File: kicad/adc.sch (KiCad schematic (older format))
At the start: 88 parts, among them IC501 TPD4E001, IC502 TPD4E001, IC503 TPD4E001, IC504 TPD4E001, IC505 TPD4E001, IC506 TPD4E001, U13_501 OPA4350EA/250, U13_502 OPA4350EA/250, U13_503 OPA4350EA/250, U13_504 OPA4350EA/250, U502 REF5030IDGKT, U503 OPA4350EA/250, U6_501 REF5030IDGKT

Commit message: usb interface changed by emu_interface
I've cleaned all the jtag interface, so the only things that go out is
jtag HOT and rx/tx isolated. I left the isolator for rx/tx cose I'm
planning to add rs485 using the same isolator and regulator, if not, I'd
clean these IC's also
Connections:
- net labels added: VDD3V3
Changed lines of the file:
@@
 EESchema Schematic File Version 4
-LIBS:servo-cache
 EELAYER 26 0
 EELAYER END
 $Descr B 17000 11000
 encoding utf-8
-Sheet 5 7
+Sheet 4 6
 Title "adc"
 Date "25 10 2019"
@@
 	10050 6200 10050 5200
 $Comp
-L servo:VDD #PWR0510
+L servo:VDD3V3 #PWR0510
 U 1 1 5DB391CF
 P 11400 2350
 F 0 "#PWR0510" H 11417 2559 20  0000 C CNN
-F 1 "VDD" H 11417 2507 30  0000 C CNN
+F 1 "VDD3V3" H 11400 2500 30  0000 C CNN
 F 2 "" H 11400 2350 70  0000 C CNN
 F 3 "" H 11400 2350 70  0000 C CNN
@@
 OPA4350EA/250
 $Comp
-L servo:VDD #PWR0516
+L servo:VDD3V3 #PWR0516
 U 1 1 5DB391CA
 P 13350 5300
@@
 $EndComp
 $Comp
-L servo:VDD #PWR0519
+L servo:VDD3V3 #PWR0519
 U 1 1 5DB391C9
 P 14550 5300
@@
 	14450 5500 14550 5500
 $Comp
-L servo:VDD #PWR0517
+L servo:VDD3V3 #PWR0517
 U 1 1 5DB391C8
 P 13350 7100
@@
 	13450 7300 13350 7300
 $Comp
-L servo:VDD #PWR0520
+L servo:VDD3V3 #PWR0520
 U 1 1 5DB391C7
 P 14550 7100
@@
 Wire Wire Line
 	14650 7700 14650 8100
-$Comp
-L servo:VDD #PWR0509
-U 1 1 5DB391C6
-P 10150 9150
-F 0 "#PWR0509" H 10167 9359 20  0000 C CNN
-F 1 "VDD" H 10167 9307 30  0000 C CNN
-F 2 "" H 10150 9150 70  0000 C CNN
-F 3 "" H 10150 9150 70  0000 C CNN
-	1    10150 9150
-	1    0    0    -1
-$EndComp
 $Comp
 L servo:GND #PWR0514
@@
 	1    0    0    -1
 $EndComp
-$Comp
-L servo:VDD #PWR0515
-U 1 1 5DB391BC
-P 12250 700
-F 0 "#PWR0515" H 12267 909 20  0000 C CNN
-F 1 "VDD" H 12267 857 30  0000 C CNN
-F 2 "" H 12250 700 70  0000 C CNN
-F 3 "" H 12250 700 70  0000 C CNN
-	1    12250 700
-	1    0    0    -1
-$EndComp
 Wire Wire Line
 	12250 800  12250 700
@@
 U 1 1 5DB391BB
 P 11450 1500
-F 0 "#PWR0512" H 11450 1640 20  0000 C CNN
-F 1 "GND" H 11450 1610 30  0000 C CNN
+F 0 "#PWR0512" H 11455 1351 20  0000 C CNN
+F 1 "GND" H 11455 1299 30  0000 C CNN
 F 2 "" H 11450 1500 70  0000 C CNN
 F 3 "" H 11450 1500 70  0000 C CNN
@@
 Wire Wire Line
 	7650 5200 3400 5200
+$Comp
+L servo:VDD3V3 #PWR0401
+U 1 1 5DE30BD8
+P 10150 9150
+F 0 "#PWR0401" H 10167 9399 50  0000 C CNN
+F 1 "VDD3V3" H 10167 9316 39  0000 C CNN
+F 2 "" H 10150 9150 50  0001 C CNN
+F 3 "" H 10150 9150 50  0001 C CNN
+	1    10150 9150
+	1    0    0    -1
+$EndComp
+$Comp
+L servo:VDD3V3 #PWR?
+U 1 1 5DED98EF
+P 12250 700
+F 0 "#PWR?" H 12255 907 20  0000 C CNN
+F 1 "VDD3V3" H 12255 857 28  0000 C CNN
+F 2 "" H 12250 700 50  0001 C CNN
+F 3 "" H 12250 700 50  0001 C CNN
+	1    12250 700
+	1    0    0    -1
+$EndComp
 $EndSCHEMATC

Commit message: power.sch added with new power 1V2, 3V3, an so global labels
I've added the power schematic and try to ojin the power label as 3V3,
VDD_3V3 an so.. keep going
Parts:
- removed C528: 0.1uF, symbol servo:Capacitor
- removed R533: 0, symbol servo:Resistor
- removed S501: W_SPDT_, symbol servo:SW_SPDT_CAS-D20TA
- removed S502: W_SPDT, symbol servo:SW_SPDT_CAS-D20TA
- removed U13_501: OPA4350EA/250, symbol servo:TI-OPA4XXX-XX16_5
- removed U13_502: OPA4350EA/250, symbol servo:TI-OPA4XXX-XX16_2
- removed U13_503: OPA4350EA/250, symbol servo:TI-OPA4XXX-XX16_4
- removed U13_504: OPA4350EA/250, symbol servo:TI-OPA4XXX-XX16_3
- removed U503: OPA4350EA/250, symbol servo:TI-OPA4XXX-XX16_1
- removed U6_501: REF5030IDGKT, symbol servo:TI-REF5030DGK8_2
- added R433, R435: 0e_np, symbol servo:Resistor
- added R434: 0e, symbol servo:Resistor
- added R436: 0, symbol servo:Resistor
- U401: renamed from U501; value ~ -> TMS320F28388DZWTS
- renumbered C501 to C401, C502 to C402, C503 to C403, C504 to C404, C505 to C405, C506 to C406, C507 to C407, C508 to C408, C509 to C409, C510 to C410, C511 to C411, C512 to C412, C513 to C413, C514 to C414, C515 to C415, C516 to C416, C517 to C417, C518 to C418, C519 to C419, C520 to C420, C521 to C421, C522 to C422, C523 to C423, C524 to C424, C525 to C425, C526 to C426, C527 to C427, C529 to C428, C530 to C429, C532 to C430, C533 to C431, C531 to C432, C534 to C433, C535 to C434, C536 to C435, C537 to C436, IC501 to IC401, IC502 to IC402, IC503 to IC403, IC504 to IC404, IC505 to IC405, IC506 to IC406, R501 to R401, R502 to R402, R503 to R403, R504 to R404, R505 to R405, R506 to R406, R507 to R407, R508 to R408, R509 to R409, R510 to R410, R511 to R411, R512 to R412, R513 to R413, R514 to R414, R515 to R415, R516 to R416, R517 to R417, R518 to R418, R519 to R419, R520 to R420, R521 to R421, R522 to R422, R523 to R423, R524 to R424, R525 to R425, R526 to R426, R527 to R427, R528 to R428, R529 to R429, R530 to R430, R531 to R431, R532 to R432, R534 to R437, R535 to R438, U502 to U402
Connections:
- net ADC_REF: now also R436.1
- net GND: now also U402.4 (GND); no longer U402.5 (TRIM/NR)
- net at U402.6 (VOUT): now also C435.1, R437.2, R438.1
- net at R429.1: now also R430.1, R431.1, R432.1, R435.2, R436.2
- net at C434.1: now also U402.5 (TRIM/NR)
- net ADC_3V0_REF: no longer names the net of U402.7 (NC)
- net VDD3V3 renamed VDDA_3V3
- net VDDA_3V3: now also R433.1, R435.1; no longer C432.1, C433.1, U402.2 (VIN)
- new net: C432.1, C433.1, R433.2, R434.2, U402.2 (VIN)
- new net IN_5V0: R434.1
- no-connect marks 6 -> 0
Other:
- note added: "For choose 5 or\n3v3 input"
- note added: "for choose btw\n3v3 and ref"
- note removed: "S3 and S4 allow a user to choose between using a clean external \nreference (such that the full-scale of the ADC is 0 to Vref, where\nVref must always be less than VDDA) or use VDDA as a reference\n(with reduced accuracy/precision)."
- moved on the sheet: C432, C433, C434, C435, C436, R430, R437, R438, U402

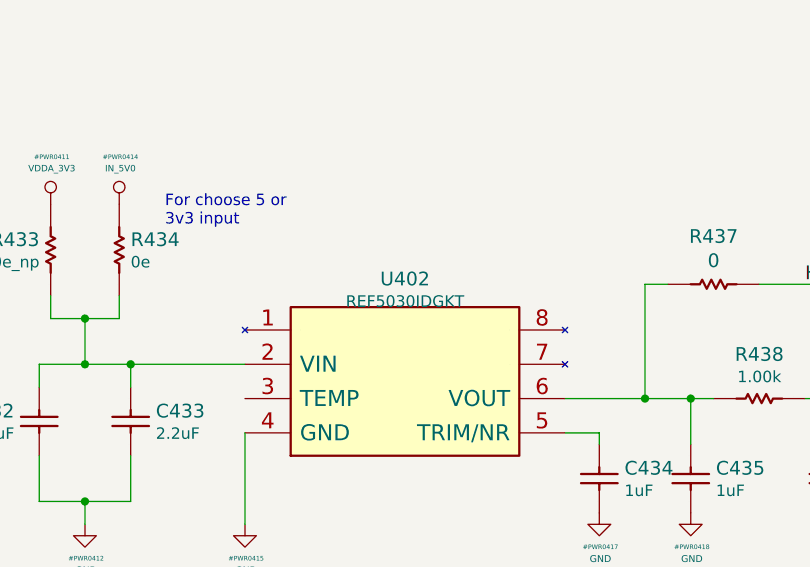
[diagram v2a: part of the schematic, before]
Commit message: clk.sch added. I'm seeing what to delete and what to keep
I've added clk.sch clk related schematics, so I'm looking to clean up
the design 'cose it has a lot of things not used in the actual design
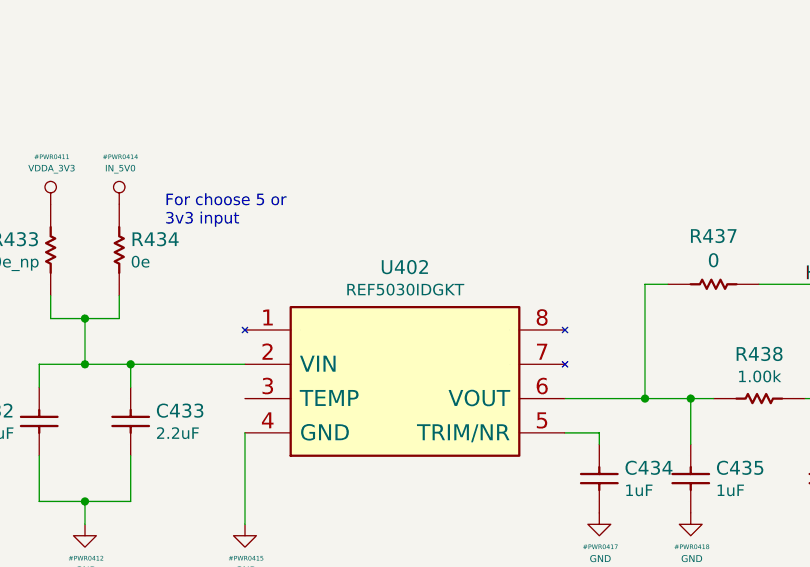
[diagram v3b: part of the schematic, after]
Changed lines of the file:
@@
 $Descr B 17000 11000
 encoding utf-8
-Sheet 4 7
+Sheet 4 8
 Title "adc"
 Date "25 10 2019"
-Rev ""
-Comp ""
-Comment1 ""
+Rev "1.0"
+Comp "dci"
+Comment1 "Pablo Slavkin"
 Comment2 ""
 Comment3 ""
@@
 U 1 1 5DB39163
 P 13500 3000
-F 0 "U402" H 13500 3473 60  0000 C CNN
-F 1 "REF5030IDGKT" H 13500 3375 50  0000 C CNN
+F 0 "U402" H 13500 3523 60  0000 C CNN
+F 1 "REF5030IDGKT" H 13500 3425 50  0000 C CNN
 F 2 "" H 13500 3000 50  0001 C CNN
 F 3 "" H 13500 3000 50  0001 C CNN

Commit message: cleaning power, added ac/dc to 15v
I've added the ac/dc power supply based on encapsulated off load power
supply and chainde linear regulator for 5, 3v3 and 1v2 for cold gnd and
5v and 3v3 for hot gnd.
I'll next join some sheet 'cose some of those are almost empty
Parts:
- removed C425, C427, C431: 22uF, symbol servo:Capacitor
- removed C434, C435: 1uF, symbol servo:Capacitor
- removed R425, R426, R427, R428: 0.1, symbol servo:Resistor
- removed R429, R430, R431, R432, R437: 0, symbol servo:Resistor
- removed R433, R435: 0e_np, symbol servo:Resistor
- removed R434: 0e, symbol servo:Resistor
- removed R438: 1.00k, symbol servo:Resistor
- removed U402: REF5030IDGKT, symbol servo:TI-REF5030DGK8_1
- R436: value 0 -> 1k
- U401: symbol servo:TMS320F28388_1 -> servo:TMS320F28388
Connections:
- net VDDA_3V3: now also C432.1, C433.1, R436.1
- net at C429.1: now also C436.1, R436.2, U401.R1 (VREFHIC), U401.V1 (VREFHIA), U401.V5 (VREFHID), U401.W5 (VREFHIB)
- removed net ADC_REF: C436.1, R436.1
- net GND renamed GNDA
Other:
- note removed: "For choose 5 or\n3v3 input"
- note removed: "If desired, isolate (or semi-isolate) alL servo:GND nets on this page\n(GNDA) from the main GND. If done, the GND terminal of C63 should\nalso go to GNDA."
- note removed: "for choose btw\n3v3 and ref"
- moved on the sheet: C429, C432, C433, C436, R436

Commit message: ok, it's enough cleaned to mix with power interface
I think it's time to mix with power interfaces.. It's enough cleaned
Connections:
- net VDDA_3V3 renamed 3V3A
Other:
- note removed: "ADC_A0A1_P and ADC_A0A1_N make a differential pair using\nchannels A0 and A1 respectivly. If you wish to use A0 or A1\nindependently the "_P" refers to the first ADC channel. For example\nA0 in "ADC_A0A1". Additionally the "_N" refers to the second\nchannel, A1 in "ADC_A0A1"."
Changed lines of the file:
@@
 EESchema Schematic File Version 4
-LIBS:servo-cache
 EELAYER 26 0
 EELAYER END
@@
 Wire Wire Line
 	1150 900  2150 900
-Text Notes 3800 9550 0    50   ~ 0
-ADC_A0A1_P and ADC_A0A1_N make a differential pair using\nchannels A0 and A1 respectivly.     If you wish to use A0 or A1\nindependently the "_P" refers to the first ADC channel. For example\nA0 in "ADC_A0A1". Additionally the "_N" refers to the second\nchannel, A1 in "ADC_A0A1".
 Connection ~ 7100 7500
 Wire Wire Line
@@
 	7650 5200 3400 5200
 $Comp
-L servo:VDDA_3V3 #PWR0413
+L servo:3V3A #PWR0413
 U 1 1 5E235B87
 P 12250 700
 F 0 "#PWR0413" H 12255 907 20  0001 C CNN
-F 1 "VDDA_3V3" H 12255 857 28  0000 C CNN
+F 1 "3V3A" H 12255 857 28  0000 C CNN
 F 2 "" H 12250 700 50  0001 C CNN
 F 3 "" H 12250 700 50  0001 C CNN
@@
 $EndComp
 $Comp
-L servo:VDDA_3V3 #PWR0416
+L servo:3V3A #PWR0416
 U 1 1 5E5CB351
 P 12000 5900
-F 0 "#PWR0416" H 12005 6107 20  0000 C CNN
-F 1 "VDDA_3V3" H 12005 6057 28  0000 C CNN
+F 0 "#PWR0416" H 12005 6107 20  0001 C CNN
+F 1 "3V3A" H 12005 6057 28  0000 C CNN
 F 2 "" H 12000 5900 50  0001 C CNN
 F 3 "" H 12000 5900 50  0001 C CNN

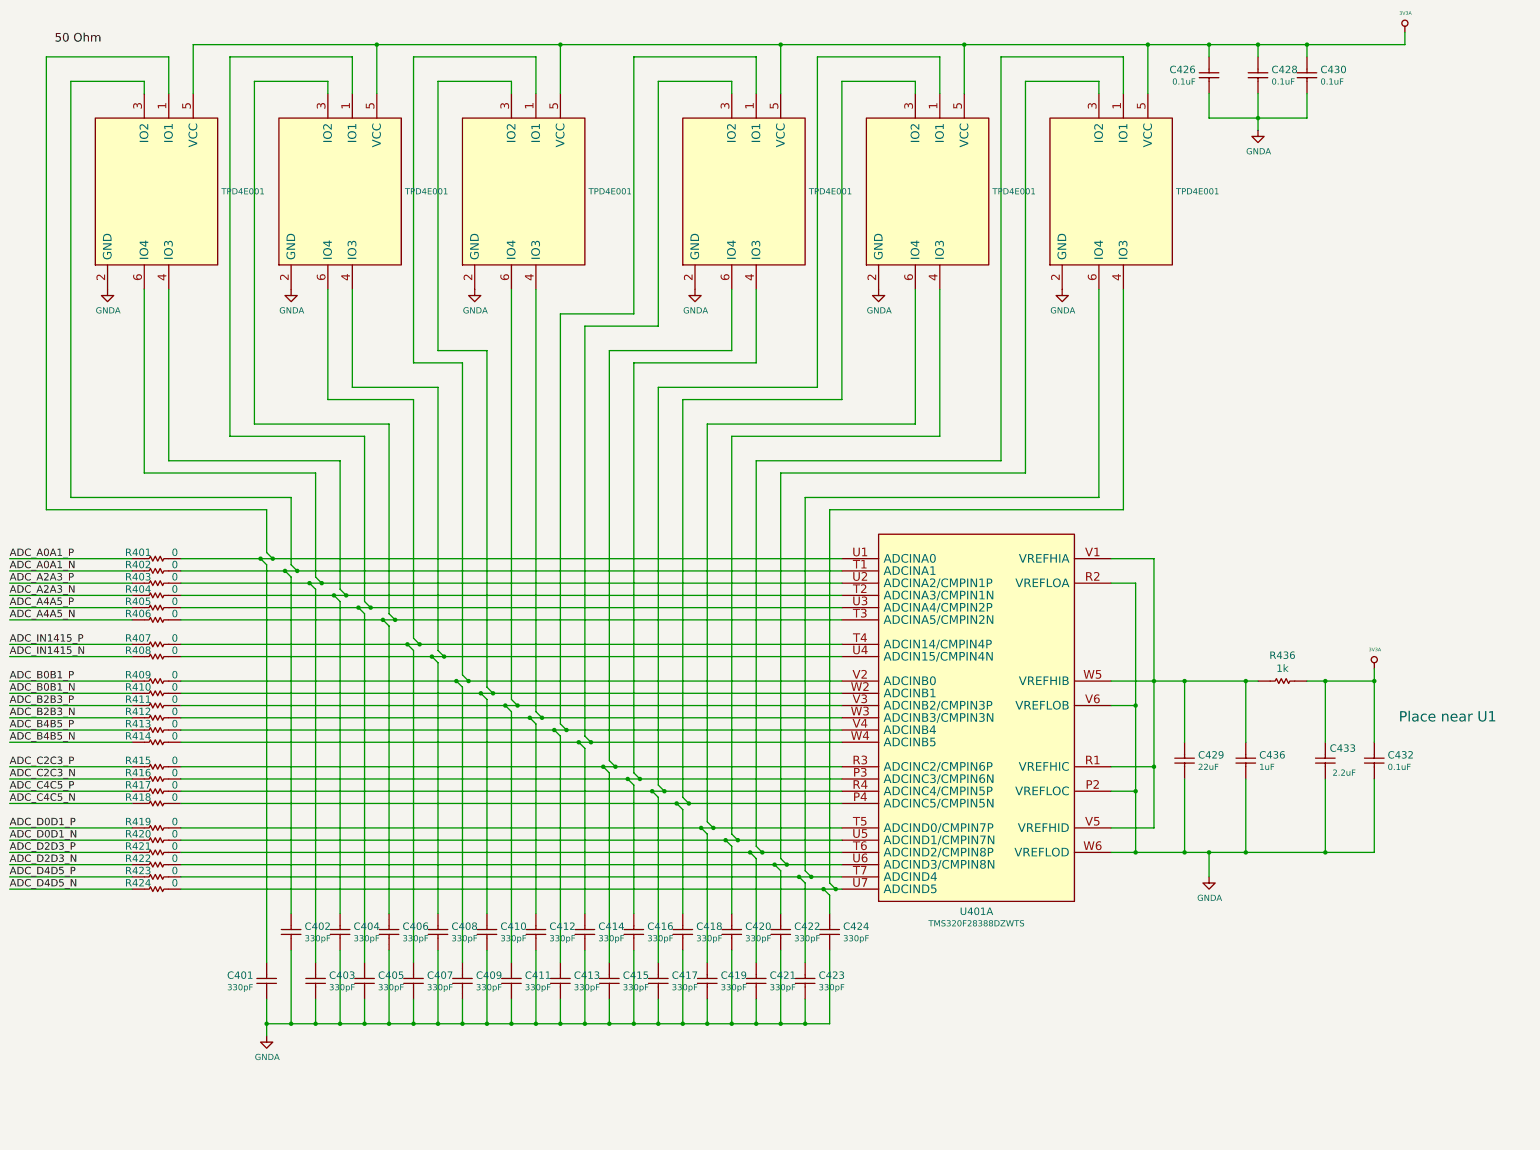
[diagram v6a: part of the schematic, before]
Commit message: added igbt interface, lem, and impprove root page
improved root page, added lem using hall sensor instead shunt, add
somthing on adc page, and ac input.. keep working
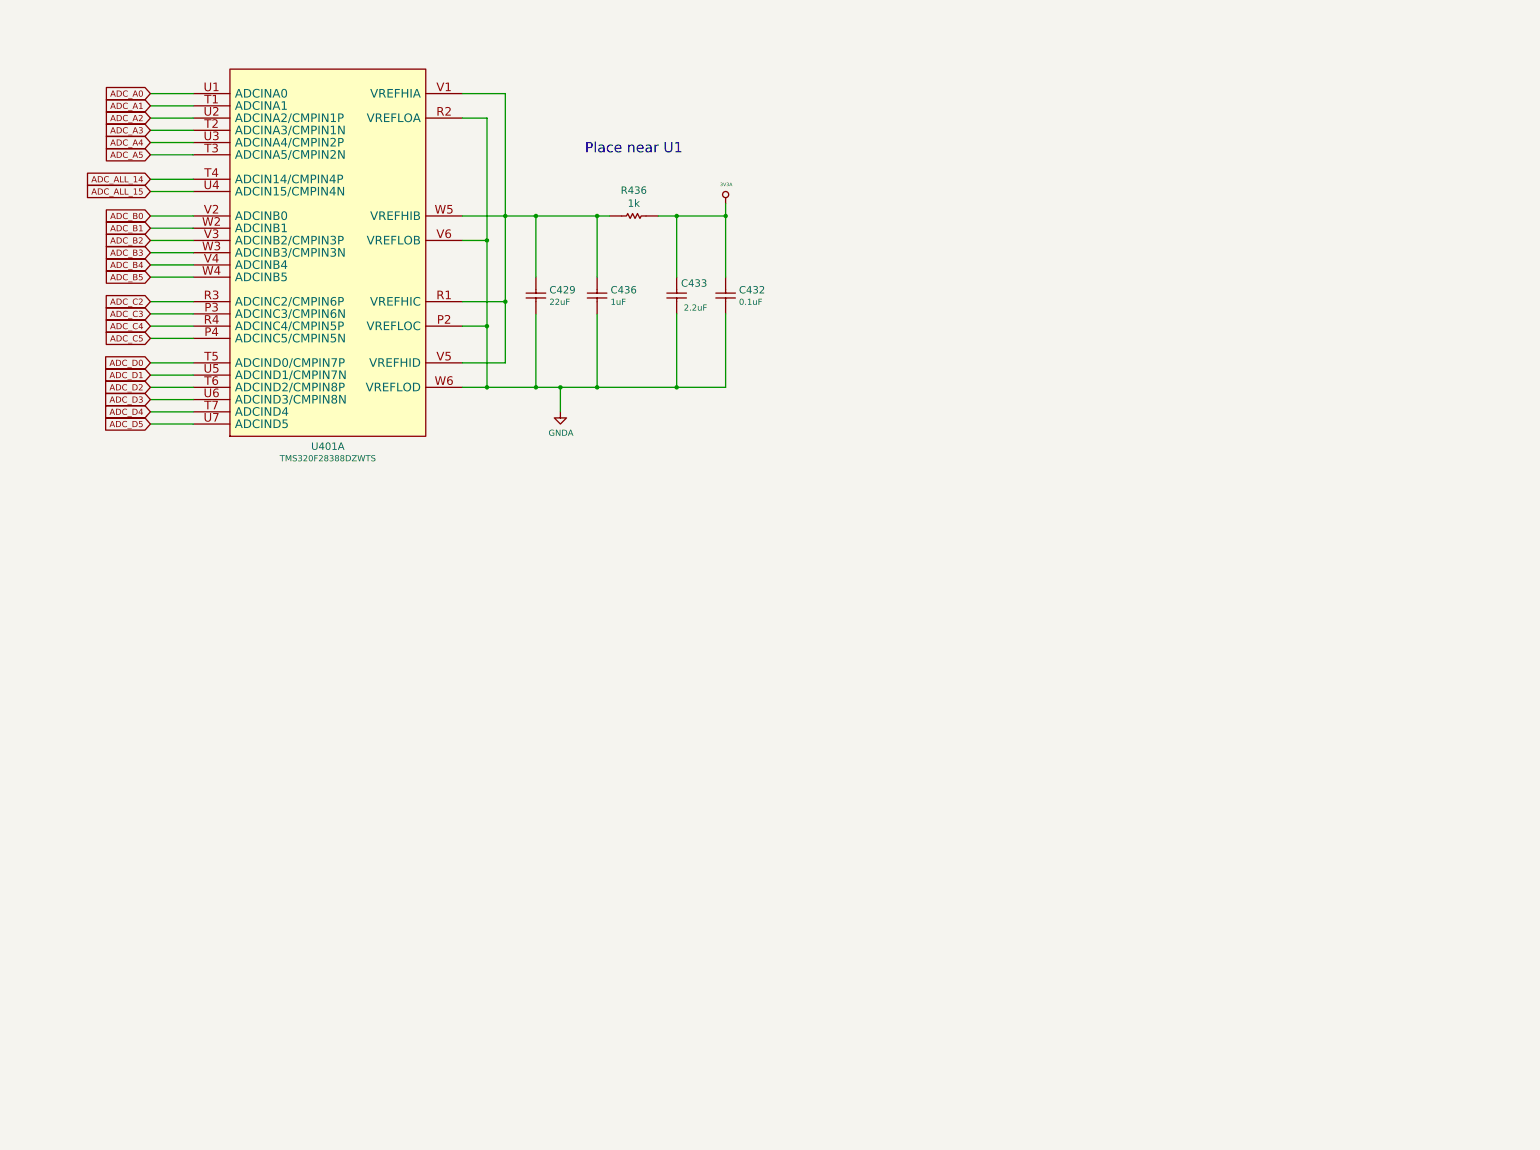
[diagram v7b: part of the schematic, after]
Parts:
- removed C401, C402, C403, C404, C405, C406, C407, C408, C409, C410, C411, C412, C413, C414, C415, C416, C417, C418, C419, C420, C421, C422, C423, C424: 330pF, symbol servo:Capacitor
- removed C426, C428, C430: 0.1uF, symbol servo:Capacitor
- removed IC401, IC402, IC403, IC404, IC405, IC406: TPD4E001, symbol servo:TPD4E001QDBV
- removed R401, R402, R403, R404, R405, R406, R407, R408, R409, R410, R411, R412, R413, R414, R415, R416, R417, R418, R419, R420, R421, R422, R423, R424: 0, symbol servo:Resistor
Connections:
- net ADC_C3: now reaches U401.P3 (ADCINC3/CMPIN6N)
- net ADC_C5: now reaches U401.P4 (ADCINC5/CMPIN5N)
- net ADC_C2: now reaches U401.R3 (ADCINC2/CMPIN6P)
- net ADC_C4: now reaches U401.R4 (ADCINC4/CMPIN5P)
- net ADC_A1: now reaches U401.T1 (ADCINA1)
- net ADC_A3: now reaches U401.T2 (ADCINA3/CMPIN1N)
- net ADC_A5: now reaches U401.T3 (ADCINA5/CMPIN2N)
- net ADC_ALL_14: now reaches U401.T4 (ADCIN14/CMPIN4P)
- net ADC_D0: now reaches U401.T5 (ADCIND0/CMPIN7P)
- net ADC_D2: now reaches U401.T6 (ADCIND2/CMPIN8P)
- net ADC_D4: now reaches U401.T7 (ADCIND4)
- net ADC_A0: now reaches U401.U1 (ADCINA0)
- net ADC_A2: now reaches U401.U2 (ADCINA2/CMPIN1P)
- net ADC_A4: now reaches U401.U3 (ADCINA4/CMPIN2P)
- net ADC_ALL_15: now reaches U401.U4 (ADCIN15/CMPIN4N)
- net ADC_D1: now reaches U401.U5 (ADCIND1/CMPIN7N)
- net ADC_D3: now reaches U401.U6 (ADCIND3/CMPIN8N)
- net ADC_D5: now reaches U401.U7 (ADCIND5)
- net ADC_B0: now reaches U401.V2 (ADCINB0)
- net ADC_B2: now reaches U401.V3 (ADCINB2/CMPIN3P)
- net ADC_B4: now reaches U401.V4 (ADCINB4)
- net ADC_B1: now reaches U401.W2 (ADCINB1)
- net ADC_B3: now reaches U401.W3 (ADCINB3/CMPIN3N)
- net ADC_B5: now reaches U401.W4 (ADCINB5)
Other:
- moved on the sheet: C429, C432, C433, C436, R436, U401A
